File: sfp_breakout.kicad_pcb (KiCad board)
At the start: 2 copper layers, 80 x 80 mm, 14 parts, among them J1 TD-, J2 TD+, J3 RD+, J4 RD-, U1 SFP

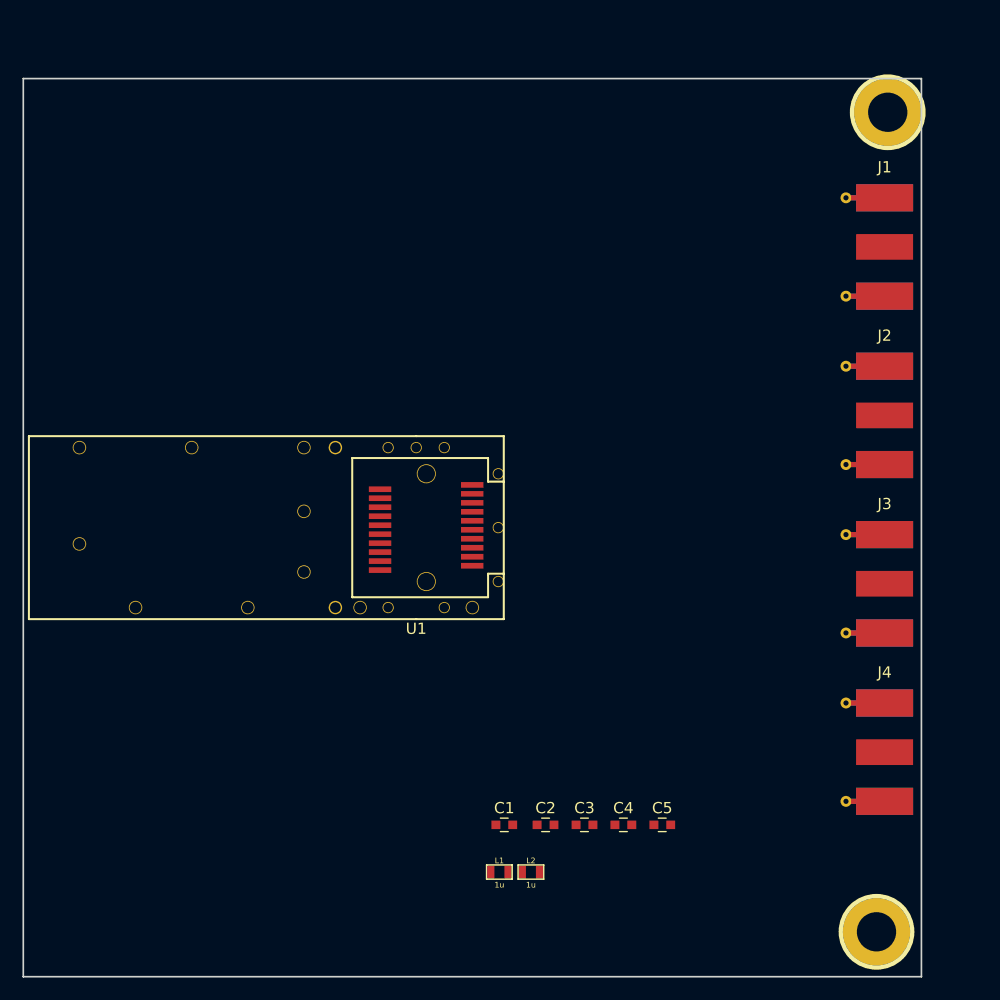
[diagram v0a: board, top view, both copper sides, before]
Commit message: Changed out SMA connector
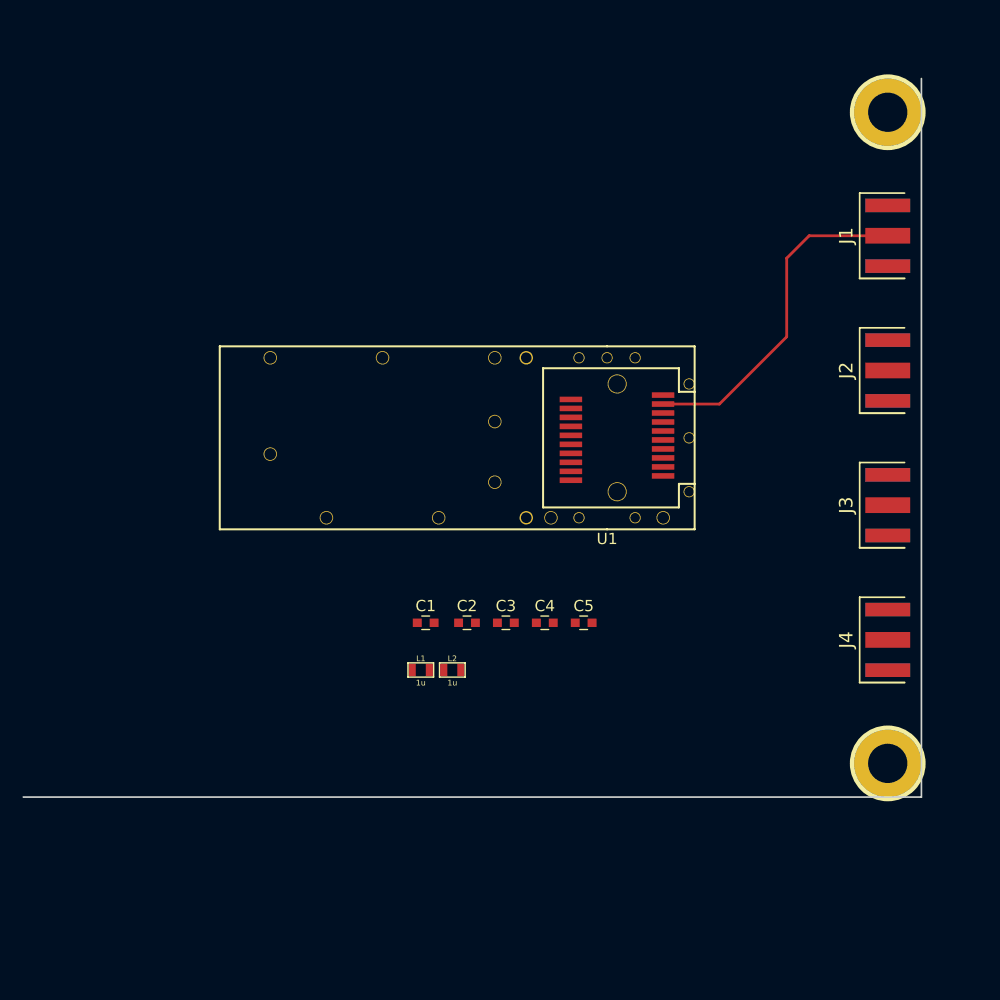
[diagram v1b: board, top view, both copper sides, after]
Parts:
- J1, J2, J3, J4: footprint Connectors_Molex:Molex_SMA_Jack_Edge_Mount -> visgence_parts:CON-SMA-EDGE
- moved C1 19.3 mm to (75.8, 88.5)
- moved C2 19.3 mm to (79.5, 88.5)
- moved C3 19.3 mm to (83.0, 88.5)
- moved C4 19.3 mm to (86.5, 88.5)
- moved C5 19.3 mm to (89.9, 88.5)
- moved L1 19.3 mm to (75.4, 92.7)
- moved L2 19.3 mm to (78.2, 92.7)
- moved U1 18.8 mm to (92.0, 72.0)
- moved h? 15.0 mm to (117.0, 101.0)
- moved J4 10.2 mm to (117.0, 90.0), turned to 270 degrees
- moved J3 7.28 mm to (117.0, 78.0), turned to 270 degrees
- moved J2 4.47 mm to (117.0, 66.0), turned to 270 degrees
- moved J1 2.24 mm to (117.0, 54.0), turned to 270 degrees
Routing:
- net TD-: track 0.00 -> 30.3 mm
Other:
- board size 80 x 80 mm -> 80 x 64 mm

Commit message: Added pin header, worked on board layout
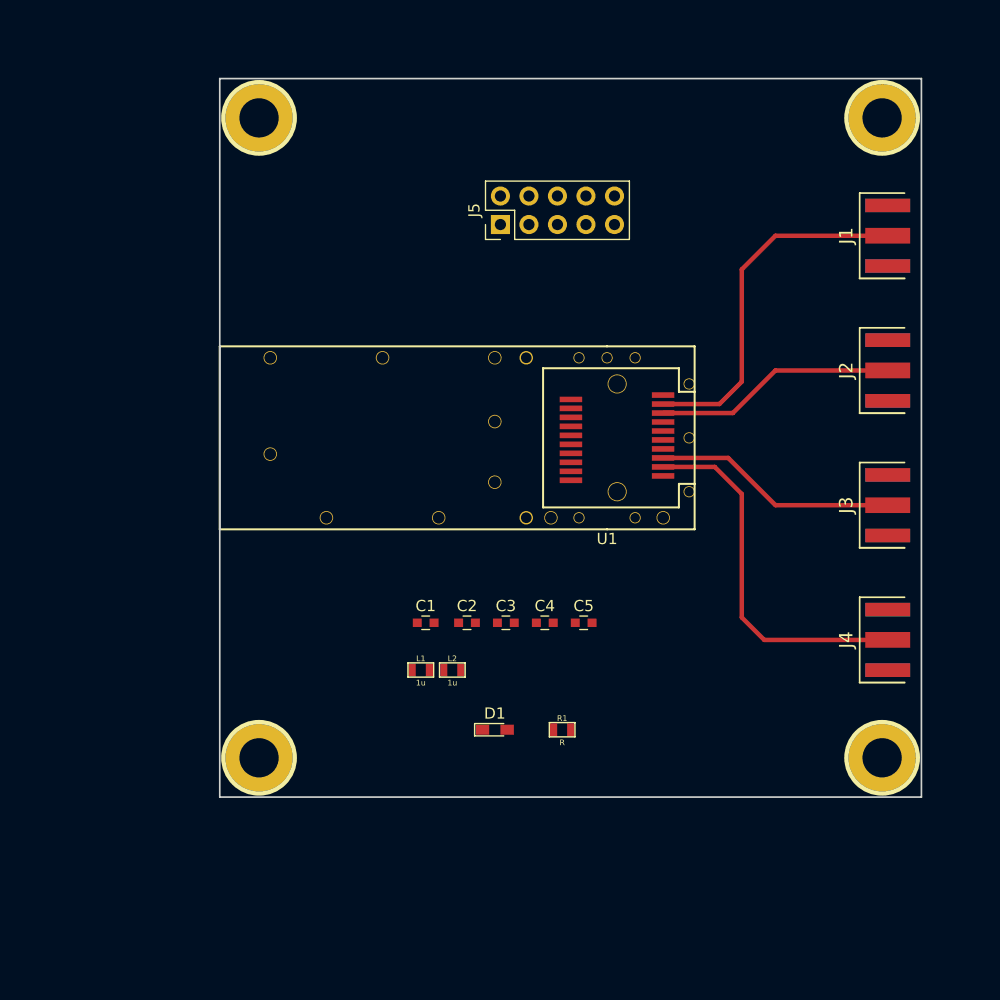
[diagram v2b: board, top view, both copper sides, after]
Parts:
- added D1: LED, LEDs:LED_0603_HandSoldering, F.Cu at (82.0, 98.0)
- added J5: Conn, Pin_Headers:Pin_Header_Straight_2x05_Pitch2.54mm, F.Cu at (82.5, 53.0)
- added R1: R, visgence_parts:SM0603_VIS, F.Cu at (88.0, 98.0)
- added h?: pin, visgence_parts:1pin_C, F.Cu at (61.0, 100.5)
- added h?: pin, visgence_parts:1pin_C, F.Cu at (61.0, 43.5)
- moved h? 0.71 mm to (116.5, 43.5)
- moved h? 0.71 mm to (116.5, 100.5)
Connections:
- U1 pad 2: Net-(U1-Pad2) -> TxFault
- U1 pad 3: Net-(U1-Pad3) -> TxDisable
- U1 pad 4: Net-(U1-Pad4) -> Def-2
- U1 pad 5: Net-(U1-Pad5) -> Def-1
- U1 pad 6: Net-(U1-Pad6) -> Def-0
- U1 pad 7: Net-(U1-Pad7) -> Rate-Sel
- U1 pad 8: Net-(U1-Pad8) -> LOS
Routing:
- net RD-: track 0.00 -> 32.8 mm
- net RD+: track 0.00 -> 21.8 mm
- net TD+: track 0.00 -> 21.6 mm
- net TD-: track 30.3 -> 32.1 mm
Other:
- board size 80 x 64 mm -> 62.5 x 64 mm
- net class Default: trace_width 0.25 -> 0.4

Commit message: Did some layout and routing
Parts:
- moved C1 22.2 mm to (98.0, 87.4), turned to 270 degrees
- moved L1 17.5 mm to (92.0, 87.0), turned to 180 degrees
- moved C3 15.9 mm to (98.0, 83.3), turned to 90 degrees
- moved C2 14.1 mm to (92.8, 83.6), turned to 90 degrees
- moved L2 13.2 mm to (91.2, 90.4), turned to 90 degrees
- moved R1 13.1 mm to (78.0, 89.6), turned to 270 degrees
- moved C5 12.9 mm to (78.0, 83.5), turned to 90 degrees
- moved D1 5.25 mm to (78.0, 94.6), turned to 90 degrees
- moved C4 5.20 mm to (88.4, 83.7), turned to 90 degrees
- moved h? 0.71 mm to (117.0, 44.0)
- moved h? 0.71 mm to (117.0, 100.0)
- moved h? 0.50 mm to (61.0, 100.0)
- moved h? 0.50 mm to (61.0, 44.0)
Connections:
- U1 pad : (no net) -> GND
- U1 pad  : (no net) -> GND
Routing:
- net +3V3: track 0.00 -> 67.2 mm, vias 0 -> 1
- net Def-2: track 0.00 -> 42.7 mm, vias 0 -> 1
- net GND: track 0.00 -> 40.1 mm
- net LOS: track 0.00 -> 38.2 mm, vias 0 -> 2
- net Def-1: track 0.00 -> 37.7 mm, vias 0 -> 1
- net Rate-Sel: track 0.00 -> 33.1 mm, vias 0 -> 2
- net Def-0: track 0.00 -> 32.2 mm, vias 0 -> 1
- net Net-(C1-Pad1): track 0.00 -> 29.0 mm, vias 0 -> 2
- net TxDisable: track 0.00 -> 23.2 mm, vias 0 -> 1
- net TxFault: track 0.00 -> 22.1 mm, vias 0 -> 1
- net Net-(C2-Pad1): track 0.00 -> 18.4 mm, vias 0 -> 2
- net Net-(D1-Pad2): track 0.00 -> 3.14 mm
- added copper zone on B.Cu, net GND
- added copper zone on F.Cu, net GND
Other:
- board size 62.5 x 64 mm -> 63 x 63 mm

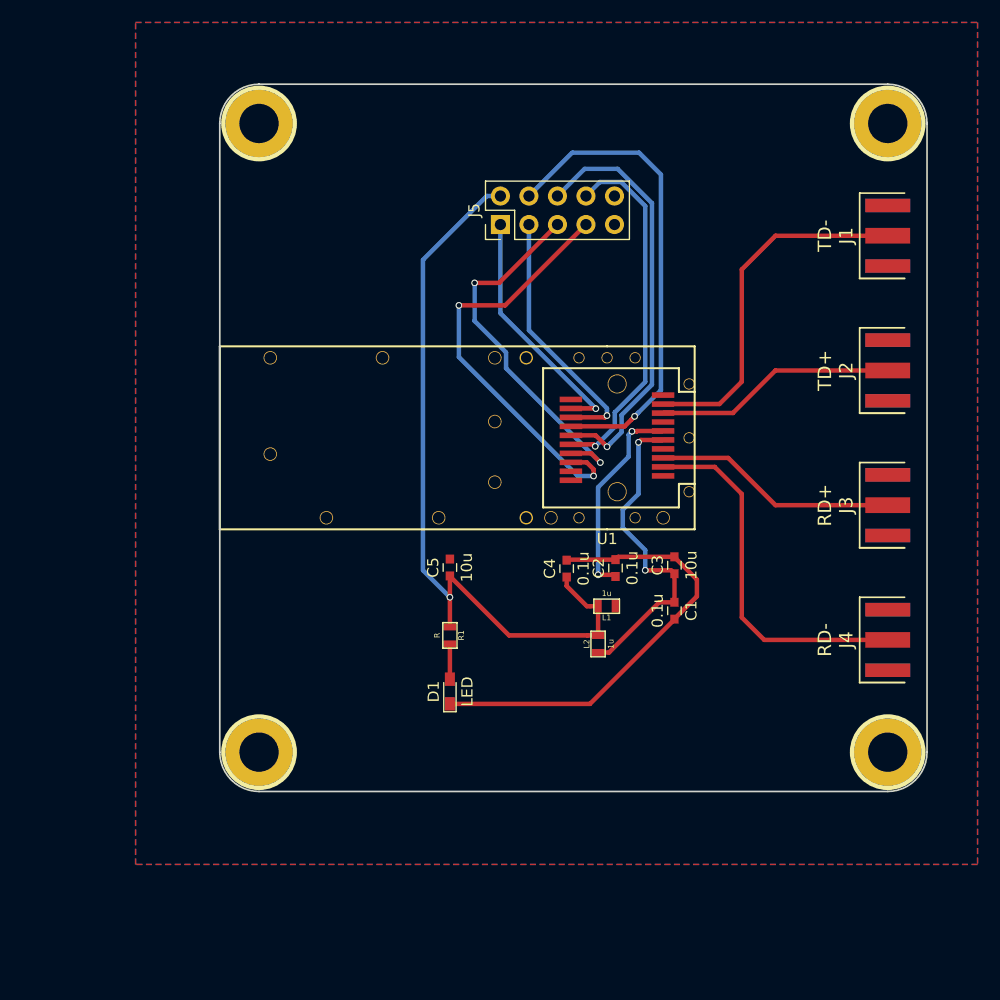
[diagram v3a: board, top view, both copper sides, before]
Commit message: Did final routing, generated gerber files
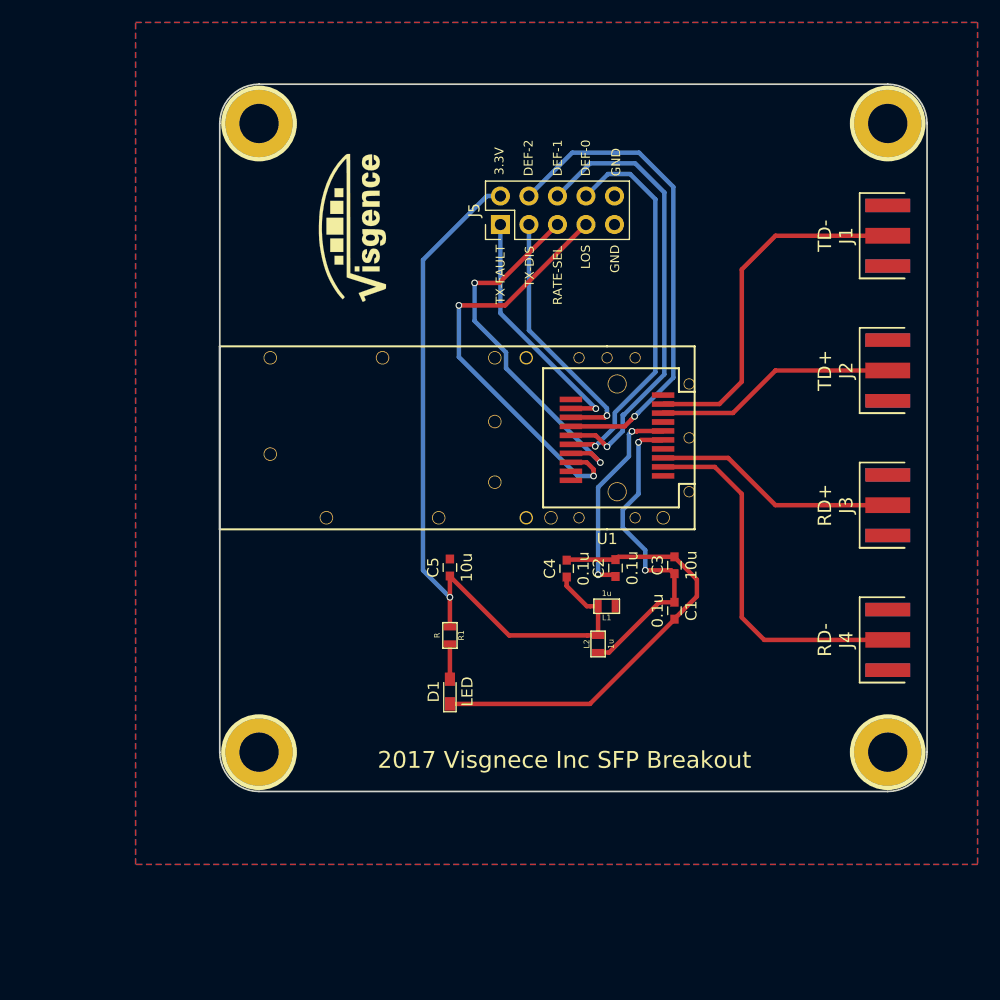
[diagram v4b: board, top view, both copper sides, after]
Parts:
- added G***: LOGO, visgence_parts:LOGO_SMALL, F.Cu at (69.3, 53.3)
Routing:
- net Def-1: track 37.7 -> 40.3 mm
- net Def-0: track 32.2 -> 34.4 mm
- net Def-2: track 42.7 -> 43.6 mm
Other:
- board text added: "2017 Visgnece Inc SFP Breakout"
- board text added: "3.3V"
- board text added: "DEF-0"
- board text added: "DEF-1"
- board text added: "DEF-2"
- board text added: "GND"
- board text added: "LOS"
- board text added: "RATE-SEL"
- board text added: "TX-DIS"
- board text added: "TX-FAULT"
